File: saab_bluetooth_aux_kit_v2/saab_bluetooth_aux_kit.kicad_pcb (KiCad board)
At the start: 2 copper layers, 88.9 x 57.2 mm, 6 parts, among them J1 Barrel_Jack, U1 MCP1703A-5002_SOT223, U2 ESP32-WROOM-30GPIO, U3 MCP2515-xST, U4 UDA1334A_BREAKOUT, U5 MCP2551-I-P

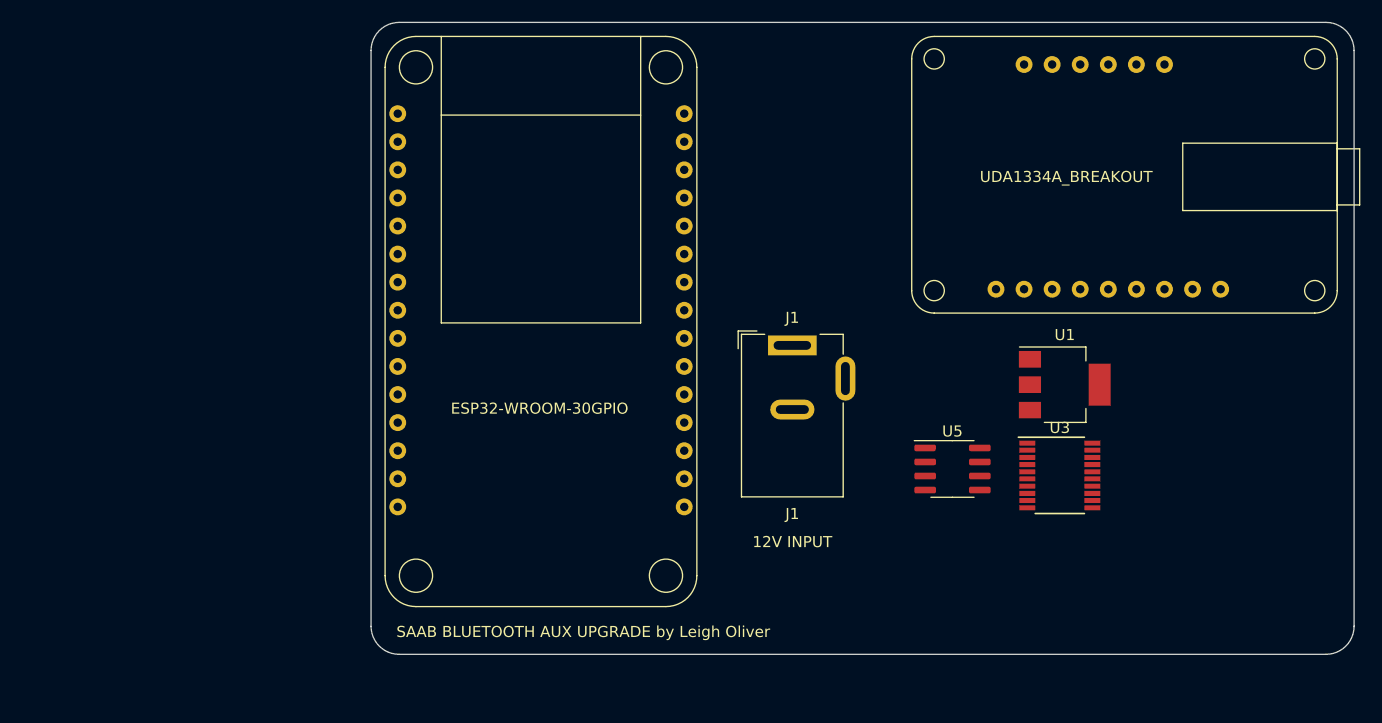
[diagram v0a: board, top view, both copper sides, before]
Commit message: Working on new bluetooth+can module from scratch
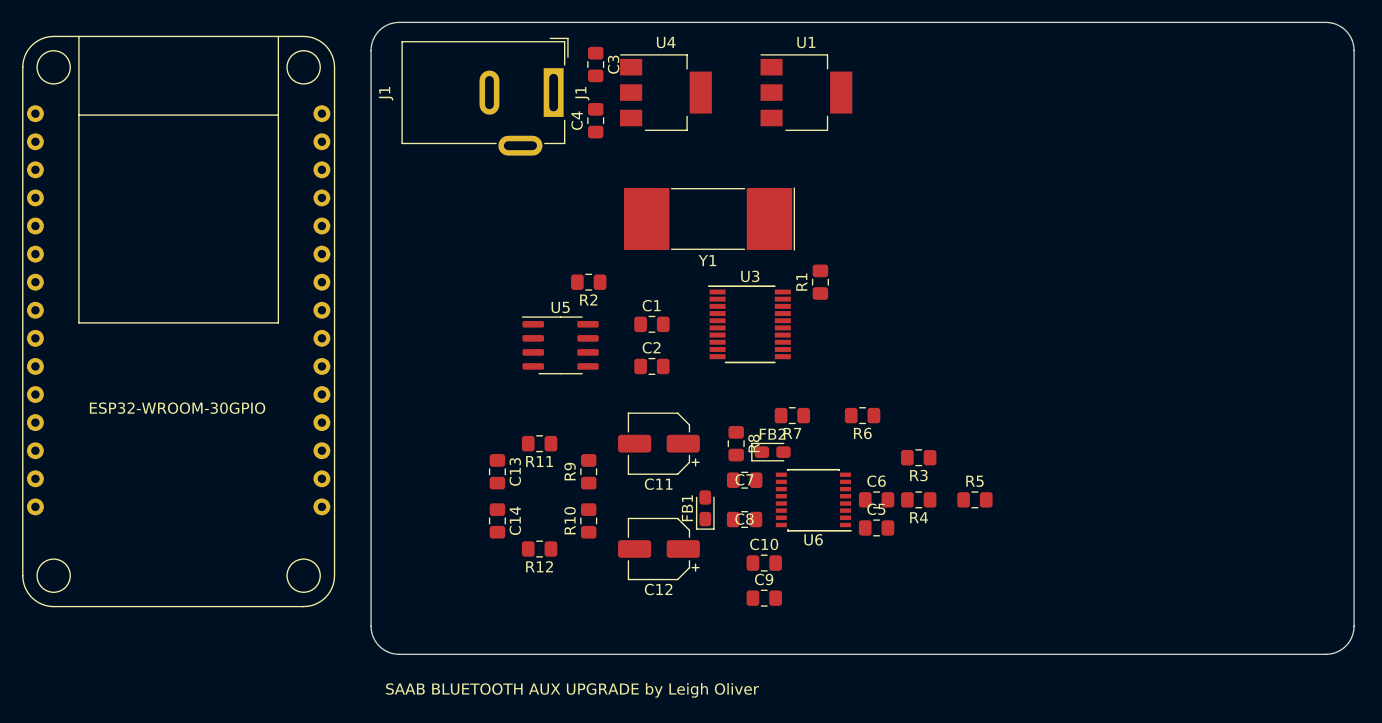
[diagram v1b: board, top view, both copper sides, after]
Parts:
- added C1: 27pF, Capacitor_SMD:C_0805_2012Metric_Pad1.15x1.40mm_HandSolder, F.Cu at (120.7, 102.2)
- added C10: 10uF, Capacitor_SMD:C_0805_2012Metric_Pad1.15x1.40mm_HandSolder, F.Cu at (130.8, 123.8)
- added C11: 47uF, Capacitor_SMD:CP_Elec_5x4.5, F.Cu at (121.3, 113.0)
- added C12: 47uF, Capacitor_SMD:CP_Elec_5x4.5, F.Cu at (121.3, 122.6)
- added C13: 0.01uF, Capacitor_SMD:C_0805_2012Metric_Pad1.15x1.40mm_HandSolder, F.Cu at (106.7, 115.6)
- added C14: 0.01uF, Capacitor_SMD:C_0805_2012Metric_Pad1.15x1.40mm_HandSolder, F.Cu at (106.7, 120.0)
- added C2: 27pF, Capacitor_SMD:C_0805_2012Metric_Pad1.15x1.40mm_HandSolder, F.Cu at (120.7, 106.0)
- added C3: 10uF, Capacitor_SMD:C_0805_2012Metric_Pad1.15x1.40mm_HandSolder, F.Cu at (115.6, 78.7)
- added C4: 10uF, Capacitor_SMD:C_0805_2012Metric_Pad1.15x1.40mm_HandSolder, F.Cu at (115.6, 83.8)
- added C5: 10uF, Capacitor_SMD:C_0805_2012Metric_Pad1.15x1.40mm_HandSolder, F.Cu at (141.0, 120.7)
- added C6: 0.1uF, Capacitor_SMD:C_0805_2012Metric_Pad1.15x1.40mm_HandSolder, F.Cu at (141.0, 118.1)
- added C7: 10uF, Capacitor_SMD:C_0805_2012Metric_Pad1.15x1.40mm_HandSolder, F.Cu at (129.0, 116.3)
- added C8: 0.1uF, Capacitor_SMD:C_0805_2012Metric_Pad1.15x1.40mm_HandSolder, F.Cu at (129.0, 119.9)
- added C9: 0.1uF, Capacitor_SMD:C_0805_2012Metric_Pad1.15x1.40mm_HandSolder, F.Cu at (130.8, 127.0)
- added FB1: Ferrite, Capacitor_Tantalum_SMD:CP_EIA-2012-12_Kemet-R_Pad1.30x1.05mm_HandSolder, F.Cu at (125.5, 118.9)
- added FB2: Ferrite, Capacitor_Tantalum_SMD:CP_EIA-2012-12_Kemet-R_Pad1.30x1.05mm_HandSolder, F.Cu at (131.6, 113.8)
- added R1: 10k, Resistor_SMD:R_0805_2012Metric_Pad1.15x1.40mm_HandSolder, F.Cu at (135.9, 98.4)
- added R10: 220k, Resistor_SMD:R_0805_2012Metric_Pad1.15x1.40mm_HandSolder, F.Cu at (114.9, 120.0)
- added R11: 100, Resistor_SMD:R_0805_2012Metric_Pad1.15x1.40mm_HandSolder, F.Cu at (110.5, 113.0)
- added R12: 100, Resistor_SMD:R_0805_2012Metric_Pad1.15x1.40mm_HandSolder, F.Cu at (110.5, 122.6)
- added R2: 10k, Resistor_SMD:R_0805_2012Metric_Pad1.15x1.40mm_HandSolder, F.Cu at (114.9, 98.4)
- added R3: 10k, Resistor_SMD:R_0805_2012Metric_Pad1.15x1.40mm_HandSolder, F.Cu at (144.8, 114.3)
- added R4: 10k, Resistor_SMD:R_0805_2012Metric_Pad1.15x1.40mm_HandSolder, F.Cu at (144.8, 118.1)
- added R5: 10k, Resistor_SMD:R_0805_2012Metric_Pad1.15x1.40mm_HandSolder, F.Cu at (149.9, 118.1)
- added R6: 10k, Resistor_SMD:R_0805_2012Metric_Pad1.15x1.40mm_HandSolder, F.Cu at (139.7, 110.5)
- added R7: 10k, Resistor_SMD:R_0805_2012Metric_Pad1.15x1.40mm_HandSolder, F.Cu at (133.3, 110.5)
- added R8: 10k, Resistor_SMD:R_0805_2012Metric_Pad1.15x1.40mm_HandSolder, F.Cu at (128.3, 113.0)
- added R9: 220k, Resistor_SMD:R_0805_2012Metric_Pad1.15x1.40mm_HandSolder, F.Cu at (114.9, 115.6)
- added U6: UDA1334ATS, Package_SO:SSOP-16_4.4x5.2mm_P0.65mm, F.Cu at (135.3, 118.1)
- added Y1: Crystal, Crystal:Crystal_SMD_SeikoEpson_MA505-2Pin_12.7x5.1mm, F.Cu at (125.7, 92.7)
- U4: value UDA1334A_BREAKOUT -> MCP1703A-3302_SOT223; footprint custom_footprints:UDA1334A-Breakout -> Package_TO_SOT_SMD:SOT-223-3_TabPin2
- moved U4 40.7 mm to (121.9, 81.3)
- moved U5 37.2 mm to (112.4, 104.1)
- moved U1 35.3 mm to (134.6, 81.3)
- moved U2 32.8 mm to (77.7, 101.6)
- moved J1 31.4 mm to (111.8, 81.3), turned to 270 degrees
- moved U3 31.2 mm to (129.5, 102.2)
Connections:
- J1 pad 1: Net-(J1-Pad1) -> VIN_12V
- U1 pad 1: Net-(J1-Pad1) -> VIN_12V
- U2 pad 3V3: 3VDC -> (no net)
- U3 pad 19: (no net) -> Net-(R1-Pad1)
- U3 pad 8: (no net) -> Net-(C1-Pad1)
- U3 pad 9: (no net) -> Net-(C2-Pad1)
- U5 pad 8: (no net) -> Net-(R2-Pad1)
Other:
- board text removed: "12V INPUT"

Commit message: Experimenting with newer DAC chips
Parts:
- removed C10, C7: 10uF, Capacitor_SMD:C_0805_2012Metric_Pad1.15x1.40mm_HandSolder
- removed C11, C12: 47uF, Capacitor_SMD:CP_Elec_5x4.5
- removed C13, C14: 0.01uF, Capacitor_SMD:C_0805_2012Metric_Pad1.15x1.40mm_HandSolder
- removed C8, C9: 0.1uF, Capacitor_SMD:C_0805_2012Metric_Pad1.15x1.40mm_HandSolder
- removed FB1, FB2: Ferrite, Capacitor_Tantalum_SMD:CP_EIA-2012-12_Kemet-R_Pad1.30x1.05mm_HandSolder
- removed R10, R9: 220k, Resistor_SMD:R_0805_2012Metric_Pad1.15x1.40mm_HandSolder
- removed R11, R12: 100, Resistor_SMD:R_0805_2012Metric_Pad1.15x1.40mm_HandSolder
- removed R6, R7, R8: 10k, Resistor_SMD:R_0805_2012Metric_Pad1.15x1.40mm_HandSolder
- added U7: MAX98357A, custom_footprints:MAX98357A, F.Cu at (131.9, 118.6)
- C4: value 10uF -> 0.1uF
- R3, R4: value 10k -> 100k
- R5: value 10k -> 210.2k
- U6: value UDA1334ATS -> MAX98357A; footprint Package_SO:SSOP-16_4.4x5.2mm_P0.65mm -> custom_footprints:MAX98357A
- moved C3 39.0 mm to (137.2, 111.3), turned to 0 degrees
- moved C4 38.0 mm to (141.9, 111.3), turned to 0 degrees
- moved R3 8.14 mm to (137.2, 117.2), turned to 0 degrees
- moved R5 8.01 mm to (141.9, 117.2)
- moved C5 7.49 mm to (137.2, 114.2)
- moved R4 7.11 mm to (146.7, 111.3), turned to 0 degrees
- moved U6 6.39 mm to (131.9, 112.7), turned to 0 degrees
- moved C6 4.02 mm to (141.9, 114.2)
- moved U4 0.51 mm to (122.4, 81.3)
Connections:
- C3 pad 1: VIN_12V -> 3.3VDC
- C4 pad 1: 3.3V -> 3.3VDC
- C5 pad 1: 3.3V -> 3.3VDC
- C6 pad 1: 3.3V -> 3.3VDC
- R3 pad 2: /UDA1334 I2S/SYSCLK_IN -> /Sheet5EEA5C09/GAIN_SEL
- R4 pad 1: GND -> /Sheet5EEA5C09/GAIN_SEL
- R4 pad 2: GND -> 3.3VDC
- R5 pad 1: GND -> 3.3VDC
- R5 pad 2: GND -> Net-(R5-Pad2)
- U4 pad 3: 3.3V -> 3.3VDC
- U6 pad 1: I2S_BCLK -> I2S_DIN
- U6 pad 10: /UDA1334 I2S/PLL0 -> (no net)
- U6 pad 12: Net-(C10-Pad1) -> (no net)
- U6 pad 13: /UDA1334 I2S/VDD_A -> (no net)
- U6 pad 14: Net-(C11-Pad1) -> I2S_WSEL
- U6 pad 15: AGND -> GND
- U6 pad 16: Net-(C12-Pad1) -> I2S_BCLK
- U6 pad 2: I2S_WSEL -> /Sheet5EEA5C09/GAIN_SEL
- U6 pad 3: I2S_DIN -> GND
- U6 pad 4: 3.3V -> 3.3VDC
- U6 pad 5: GND -> (no net)
- U6 pad 6: /UDA1334 I2S/SYSCLK_IN -> (no net)
- U6 pad 7: GND -> 3.3VDC
- U6 pad 8: /UDA1334 I2S/MUTE -> 3.3VDC
- U6 pad 9: /UDA1334 I2S/DEEM -> (no net)
